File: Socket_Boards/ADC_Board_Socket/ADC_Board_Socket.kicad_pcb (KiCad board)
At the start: 4 copper layers, 64.1 x 13.6 mm, 23 parts

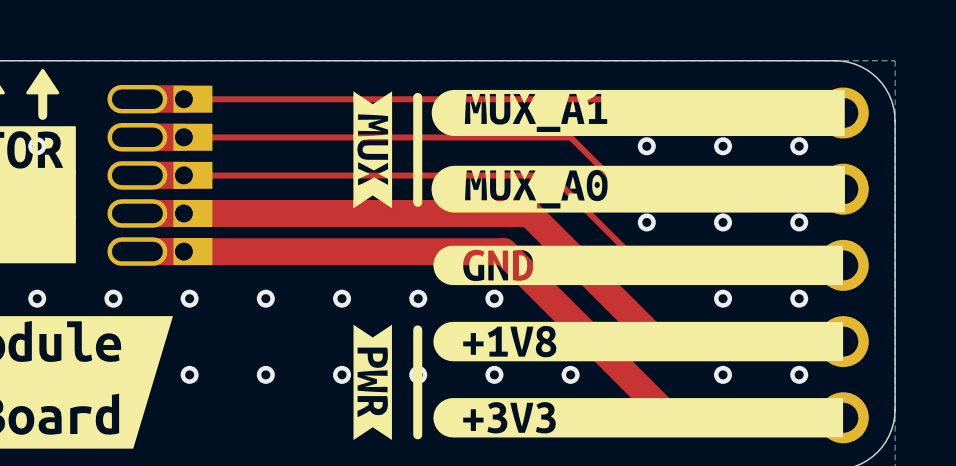
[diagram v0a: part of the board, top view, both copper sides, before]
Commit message: Fixed bugs. Added comments. Push before changing the ADC
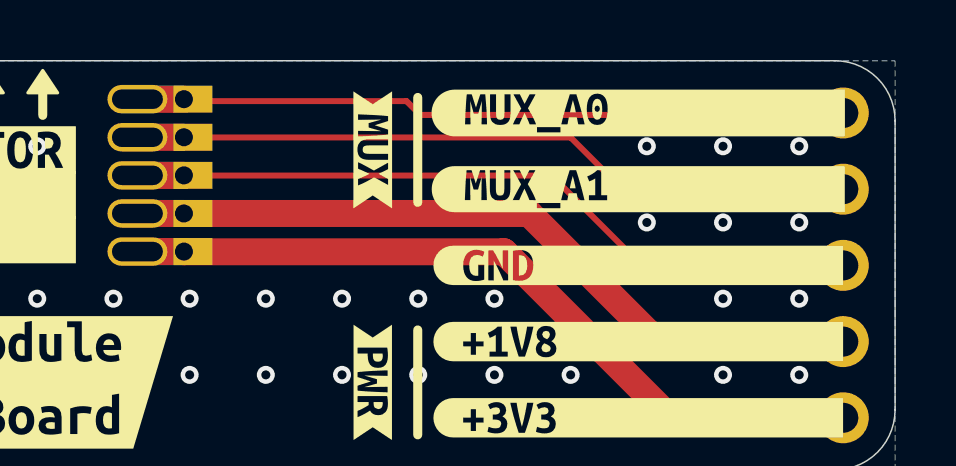
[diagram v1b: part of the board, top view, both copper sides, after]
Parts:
- removed kibuzzard-67167169: G***, kibuzzard-67167169
- removed kibuzzard-6716716F: G***, kibuzzard-6716716F
- added kibuzzard-674D70C4: G***, kibuzzard-674D70C4, F.Cu at (165.1, 96.5)
- added kibuzzard-674D70CB: G***, kibuzzard-674D70CB, F.Cu at (165.1, 99.1)
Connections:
- net Net-(J1B-MUX_A0) renamed /MUX_A1
- net Net-(J1B-MUX_A1) renamed /MUX_A0

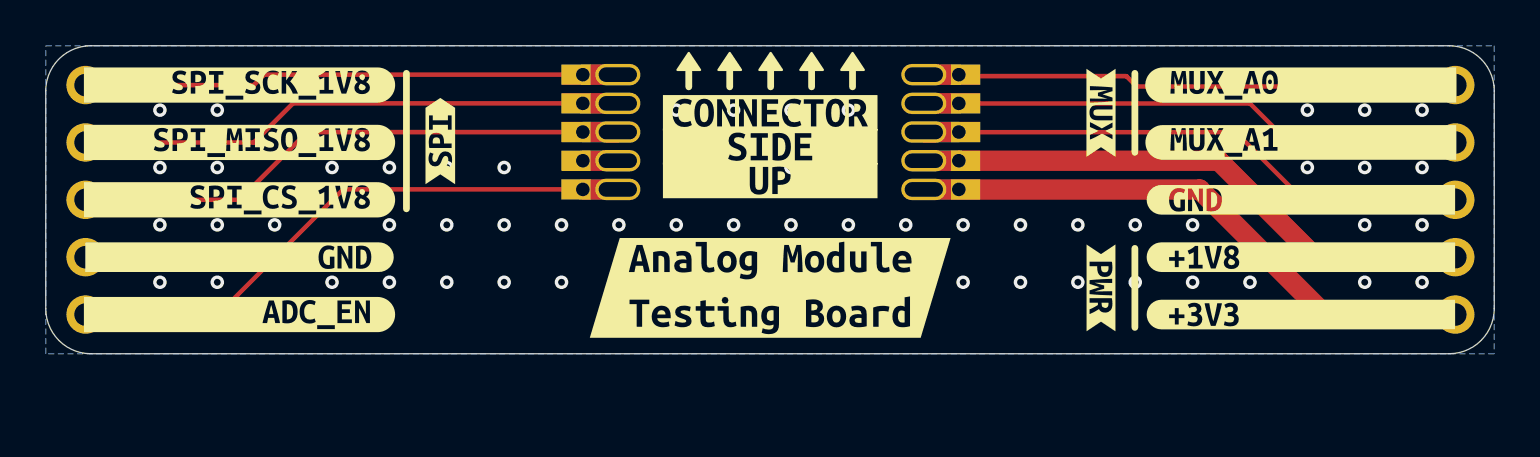
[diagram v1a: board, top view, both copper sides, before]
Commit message: Added new version of the ADC Board. Better ADC, precision reference. Similar power consumption
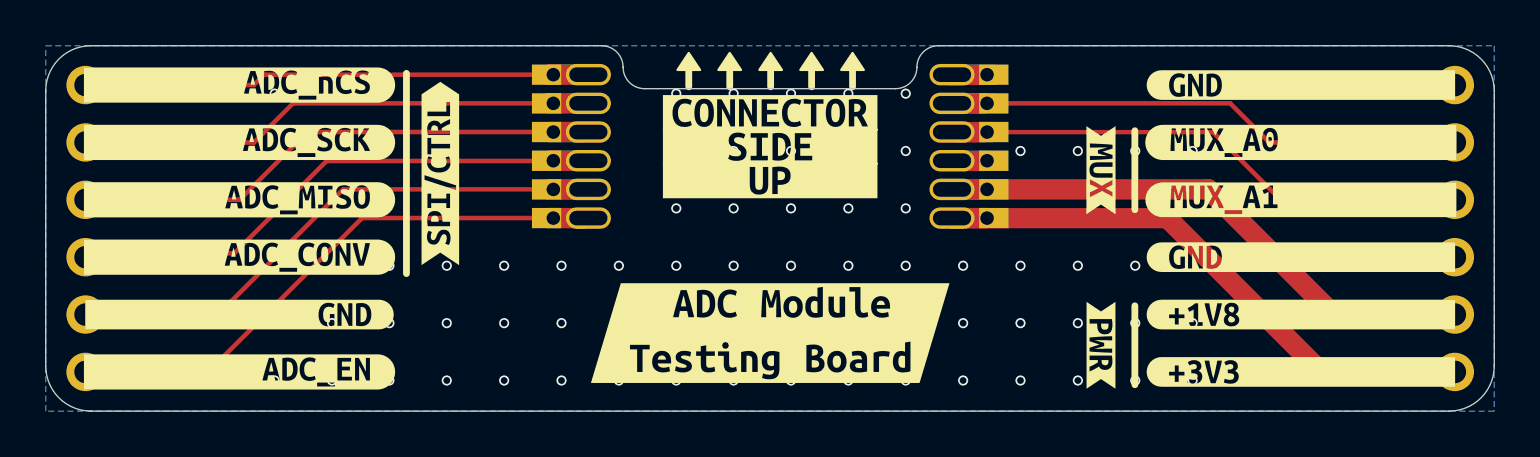
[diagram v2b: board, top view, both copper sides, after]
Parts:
- removed kibuzzard-66CFD049: G***, kibuzzard-66CFD049
- removed kibuzzard-66E729F7: G***, kibuzzard-66E729F7
- removed kibuzzard-67167147: G***, kibuzzard-67167147
- removed kibuzzard-67167151: G***, kibuzzard-67167151
- removed kibuzzard-67167155: G***, kibuzzard-67167155
- removed kibuzzard-6716715A: G***, kibuzzard-6716715A
- removed kibuzzard-6716715F: G***, kibuzzard-6716715F
- removed kibuzzard-67167174: G***, kibuzzard-67167174
- removed kibuzzard-67167178: G***, kibuzzard-67167178
- removed kibuzzard-6716717D: G***, kibuzzard-6716717D
- removed kibuzzard-6717D529: G***, kibuzzard-6717D529
- removed kibuzzard-674D70C4: G***, kibuzzard-674D70C4
- removed kibuzzard-674D70CB: G***, kibuzzard-674D70CB
- added kibuzzard-675213DB: G***, kibuzzard-675213DB, F.Cu at (118.1, 96.5)
- added kibuzzard-675213E4: G***, kibuzzard-675213E4, F.Cu at (118.1, 99.1)
- added kibuzzard-675213ED: G***, kibuzzard-675213ED, F.Cu at (118.1, 101.6)
- added kibuzzard-675213F9: G***, kibuzzard-675213F9, F.Cu at (118.1, 104.1)
- added kibuzzard-67521402: G***, kibuzzard-67521402, F.Cu at (118.1, 106.7)
- added kibuzzard-6752142A: G***, kibuzzard-6752142A, F.Cu at (118.1, 109.2)
- added kibuzzard-67521439: G***, kibuzzard-67521439, F.Cu at (165.1, 96.5)
- added kibuzzard-67521441: G***, kibuzzard-67521441, F.Cu at (165.1, 99.1)
- added kibuzzard-67521447: G***, kibuzzard-67521447, F.Cu at (165.1, 101.6)
- added kibuzzard-6752145A: G***, kibuzzard-6752145A, F.Cu at (165.1, 104.1)
- added kibuzzard-67521463: G***, kibuzzard-67521463, F.Cu at (165.1, 106.7)
- added kibuzzard-67521485: G***, kibuzzard-67521485, F.Cu at (165.1, 109.2)
- added kibuzzard-675214A3: G***, kibuzzard-675214A3, F.Cu at (127.0, 100.4)
- added kibuzzard-67521825: G***, kibuzzard-67521825, F.Cu at (141.6, 107.5)
- added kibuzzard-675218DD: G***, kibuzzard-675218DD, B.Cu at (120.5, 105.3)
- moved J2 5.42 mm to (141.6, 93.2)
- moved kibuzzard-6717DE61 2.54 mm to (156.2, 108.0)
- moved kibuzzard-6717DE83 2.54 mm to (156.2, 100.3)
- moved G*** 1.27 mm to (120.5, 98.9)
- moved J1 1.27 mm to (141.6, 102.9)
- moved G*** 1.27 mm to (161.7, 101.8)
- moved kibuzzard-66CFCF0D 1.27 mm to (161.7, 107.8)
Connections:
- J1 pad 10: /MUX_A0 -> /MUX_A1
- J1 pad 4: GND -> Net-(J1A-ADC_CONV)
- J1 pad 5: Net-(J1A-ADC_EN) -> GND
- J1 pad 6: +3.3V -> Net-(J1A-ADC_EN)
- J1 pad 7: +1V8 -> +3.3V
- J1 pad 8: GND -> +1V8
- J1 pad 9: /MUX_A1 -> GND
- J2 pad 10: /MUX_A0 -> /MUX_A1
- J2 pad 4: GND -> Net-(J1A-ADC_CONV)
- J2 pad 5: Net-(J1A-ADC_EN) -> GND
- J2 pad 6: +3.3V -> Net-(J1A-ADC_EN)
- J2 pad 7: +1V8 -> +3.3V
- J2 pad 8: GND -> +1V8
- J2 pad 9: /MUX_A1 -> GND
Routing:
- net Net-(J1A-ADC_CONV): track 0.00 -> 28.6 mm
- net Net-(J1A-ADC_EN): track 32.1 -> 26.6 mm
- net GND: track 37.2 -> 41.6 mm, vias 63 -> 76
- net Net-(J1A-ADC_SCK): track 30.5 -> 27.6 mm
- net Net-(J1A-ADC_MISO): track 31.0 -> 28.2 mm
- net +3.3V: track 30.6 -> 27.9 mm
- net /MUX_A1: track 30.5 -> 28.4 mm
- net /MUX_A0: track 28.4 -> 27.6 mm
- net +1V8: track 29.9 -> 30.5 mm
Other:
- board size 64.1 x 13.6 mm -> 64.1 x 16.2 mm

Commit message: Final revision and production files
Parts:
- removed kibuzzard-6717DF50: G***, kibuzzard-6717DF50
- removed kibuzzard-6717DF55: G***, kibuzzard-6717DF55
- removed kibuzzard-6717DF5A: G***, kibuzzard-6717DF5A
- removed kibuzzard-675218DD: G***, kibuzzard-675218DD
- added kibuzzard-67530B9C: G***, kibuzzard-67530B9C, B.Cu at (120.5, 105.3)
- added kibuzzard-67530DEF: G***, kibuzzard-67530DEF, F.Cu at (141.6, 99.8)
- added kibuzzard-67530DF3: G***, kibuzzard-67530DF3, F.Cu at (141.6, 100.9)
- added kibuzzard-67530DF9: G***, kibuzzard-67530DF9, F.Cu at (141.6, 102.1)
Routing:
- net GND: vias 76 -> 71
